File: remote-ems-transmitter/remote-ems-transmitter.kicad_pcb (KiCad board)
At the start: 2 copper layers, 65 x 30 mm, 59 parts, among them IC1 Wio-E5, J1 Conn_01x04_Pin, J2 Conn_01x02, J3 Conn_01x02, J4 Conn_Coaxial, J5 USB_C_Receptacle_USB2.0, J6 Conn_01x02_Pin, Q1 BSS138, SW1 SW_Push, SW2 SW_Push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

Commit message: LED周り修正
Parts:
- removed R21: 1k, Resistor_SMD:R_0603_1608Metric_Pad0.98x0.95mm_HandSolder
- added BAR2: OSX40601-AO, 0Ikedalibrary:OSX40601-AO, B.Cu at (36.1, 23.1)
- added D2: LED, LED_THT:LED_D5.0mm_FlatTop, B.Cu at (26.9, 35.7)
- BAR1: value HDSP-4830_2 -> OSX05201-GGR1; footprint Display:HDSP-4830 -> 0Ikedalibrary:OSX05201-GGR1
- D1: footprint LED_SMD:LED_0603_1608Metric_Pad1.05x0.95mm_HandSolder -> LED_THT:LED_D5.0mm_FlatTop
- R3: value 4.7k -> 100; moved to B.Cu
- SW4: moved to B.Cu
- moved R3 34.0 mm to (63.0, 36.4), turned to 0 degrees
- moved D1 22.6 mm to (37.7, 35.7), turned to 90 degrees
- moved J6 14.2 mm to (27.1, 29.5)
- moved BAR1 11.7 mm to (44.2, 22.4)
- moved C11 9.43 mm to (29.0, 43.4), turned to 180 degrees
- moved R4 7.85 mm to (42.4, 24.0), turned to 0 degrees
- moved R11 6.41 mm to (42.4, 25.6), turned to 0 degrees
- moved C14 5.20 mm to (20.6, 29.6)
- moved C15 5.20 mm to (20.6, 36.0)
- moved U5 5.00 mm to (20.8, 32.8)
- moved U3 4.93 mm to (29.0, 40.2), turned to -90 degrees
- moved C12 4.84 mm to (17.2, 29.6)
- moved C13 4.84 mm to (17.2, 36.0)
- moved U4 4.84 mm to (17.1, 32.8)
- moved R19 4.57 mm to (37.2, 30.8), turned to 0 degrees
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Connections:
- BAR1 pad 10: LED_opt_supply9 -> Net-(BAR1-K-Pad10)
- BAR1 pad 6: LED_opt_supply5 -> Net-(BAR1-K-Pad6)
- BAR1 pad 7: LED_opt_supply6 -> Net-(BAR1-K-Pad7)
- BAR1 pad 8: LED_opt_supply7 -> Net-(BAR1-K-Pad8)
- BAR1 pad 9: LED_opt_supply8 -> Net-(BAR1-K-Pad9)
- D1 pad 2: Net-(D1-A) -> VBUS
- Q1 pad 1: Wio-RST -> Net-(Q1-G)
- R11 pad 1: Net-(BAR1-K-Pad13) -> Net-(BAR2-K-Pad6)
- R11 pad 2: GNDD -> SW
- R12 pad 1: Net-(BAR1-K-Pad14) -> Net-(BAR2-A-Pad4)
- R12 pad 2: GNDD -> SW
- R13 pad 1: Net-(BAR1-K-Pad15) -> Net-(BAR2-A-Pad2)
- R13 pad 2: GNDD -> SW
- R14 pad 1: Net-(BAR1-K-Pad16) -> Net-(BAR1-K-Pad6)
- R15 pad 1: Net-(BAR1-K-Pad17) -> Net-(BAR1-K-Pad7)
- R16 pad 1: Net-(BAR1-K-Pad18) -> Net-(BAR1-K-Pad8)
- R17 pad 1: Net-(BAR1-K-Pad19) -> Net-(BAR1-K-Pad9)
- R18 pad 1: Net-(BAR1-K-Pad20) -> Net-(BAR1-K-Pad10)
- R3 pad 1: Net-(BAR1-K-Pad11) -> Wio-RST
- R3 pad 2: GNDD -> Net-(Q1-G)
- R4 pad 1: Net-(BAR1-K-Pad12) -> Net-(BAR2-K-Pad8)
- R4 pad 2: GNDD -> SW
- R8 pad 1: Wio-RST -> Net-(Q1-G)
- U1 pad 20: LED_opt_supply5 -> unconnected-(U1-PA10-Pad20)
- U1 pad 21: LED_opt_supply6 -> unconnected-(U1-PA11-Pad21)
- U1 pad 22: LED_opt_supply7 -> unconnected-(U1-PA12-Pad22)
- U1 pad 25: LED_opt_supply9 -> unconnected-(U1-PA15-Pad25)
- U1 pad 26: LED_opt_supply8 -> unconnected-(U1-PB3-Pad26)
- U1 pad 28: LED2 -> unconnected-(U1-PB5-Pad28)
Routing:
- net +3.3V: track 86.6 -> 137.3 mm
- net SW: track 20.8 -> 42.8 mm, vias 0 -> 2
- net LED1: track 0.00 -> 18.0 mm, vias 0 -> 2
- net UART_RX: track 8.77 -> 24.8 mm, vias 0 -> 1
- net LED_opt_supply8: track 15.7 -> 0.00 mm, vias 1 -> 0
- net LED_opt_supply9: track 15.5 -> 0.00 mm, vias 1 -> 0
- net UART_TX: track 6.91 -> 22.0 mm, vias 0 -> 1
- net LED_opt_supply7: track 12.7 -> 0.00 mm
- net LED_opt_supply6: track 11.0 -> 0.00 mm
- net Net-(BAR2-K-Pad8): track 0.00 -> 10.4 mm
- net STAT: track 18.3 -> 7.96 mm, vias 1 -> 2
- net LED_opt_supply5: track 9.24 -> 0.00 mm
- net +BATT: track 44.0 -> 52.0 mm
- net Net-(BAR2-A-Pad2): track 0.00 -> 7.93 mm
- net Wio-RST: track 22.3 -> 16.8 mm
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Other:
- board text added: "R T"
- board text added: "RST"
- board text added: "UART"

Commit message: LED仕様変更
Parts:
- added Q2: BSS138, Package_TO_SOT_SMD:SOT-23, F.Cu at (41.6, 30.6)
- added R21: 100, Resistor_SMD:R_0603_1608Metric_Pad0.98x0.95mm_HandSolder, F.Cu at (45.3, 30.5)
- added R22: 10k, Resistor_SMD:R_0603_1608Metric_Pad0.98x0.95mm_HandSolder, F.Cu at (45.3, 28.9)
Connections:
- BAR2 pad 3: +3.3V -> Net-(BAR2-A-Pad3)
- BAR2 pad 4: Net-(BAR2-A-Pad4) -> +3.3V
- BAR2 pad 7: +3.3V -> Net-(BAR2-K-Pad7)
- BAR2 pad 8: Net-(BAR2-K-Pad8) -> +3.3V
- R11 pad 2: SW -> Net-(Q2-S)
- R12 pad 1: Net-(BAR2-A-Pad4) -> Net-(BAR2-A-Pad3)
- R12 pad 2: SW -> Net-(Q2-S)
- R13 pad 2: SW -> Net-(Q2-S)
- R4 pad 1: Net-(BAR2-K-Pad8) -> Net-(BAR2-K-Pad7)
- R4 pad 2: SW -> Net-(Q2-S)
- U1 pad 20: unconnected-(U1-PA10-Pad20) -> emergency_stop_LED
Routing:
- net SW: track 42.8 -> 20.8 mm, vias 2 -> 0
- net Net-(BAR2-K-Pad8): track 10.4 -> 0.00 mm
- net Net-(Q2-S): track 0.00 -> 9.17 mm
- net Net-(BAR2-K-Pad7): track 0.00 -> 7.86 mm
- net Net-(BAR2-A-Pad3): track 0.00 -> 4.74 mm
- net Net-(Q2-G): track 0.00 -> 3.88 mm
- net emergency_stop_LED: track 0.00 -> 2.52 mm
- net Net-(BAR2-A-Pad4): track 2.20 -> 0.00 mm
- net +3.3V: track 137.3 -> 138.8 mm
- net GNDD: vias 37 -> 41

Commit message: ビア打ち、シルク修正中　残りは別日に対応します
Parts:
- added D3: LED, LED_SMD:LED_0603_1608Metric_Pad1.05x0.95mm_HandSolder, F.Cu at (29.4, 41.6)
- added G***: LOGO, LOGO, B.Cu at (66.2, 22.4)
- added R23: 1k, Resistor_SMD:R_0603_1608Metric_Pad0.98x0.95mm_HandSolder, F.Cu at (29.4, 38.2)
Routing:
- net VBUS: track 38.1 -> 42.9 mm
- net Net-(D3-A): track 0.00 -> 1.61 mm
- net GNDD: vias 41 -> 106
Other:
- board text added: "LED"
- board text added: "USB"
- board text added: "remote-ems-transmitter version 1.0 create by ikeda"
- board text added: "充電"

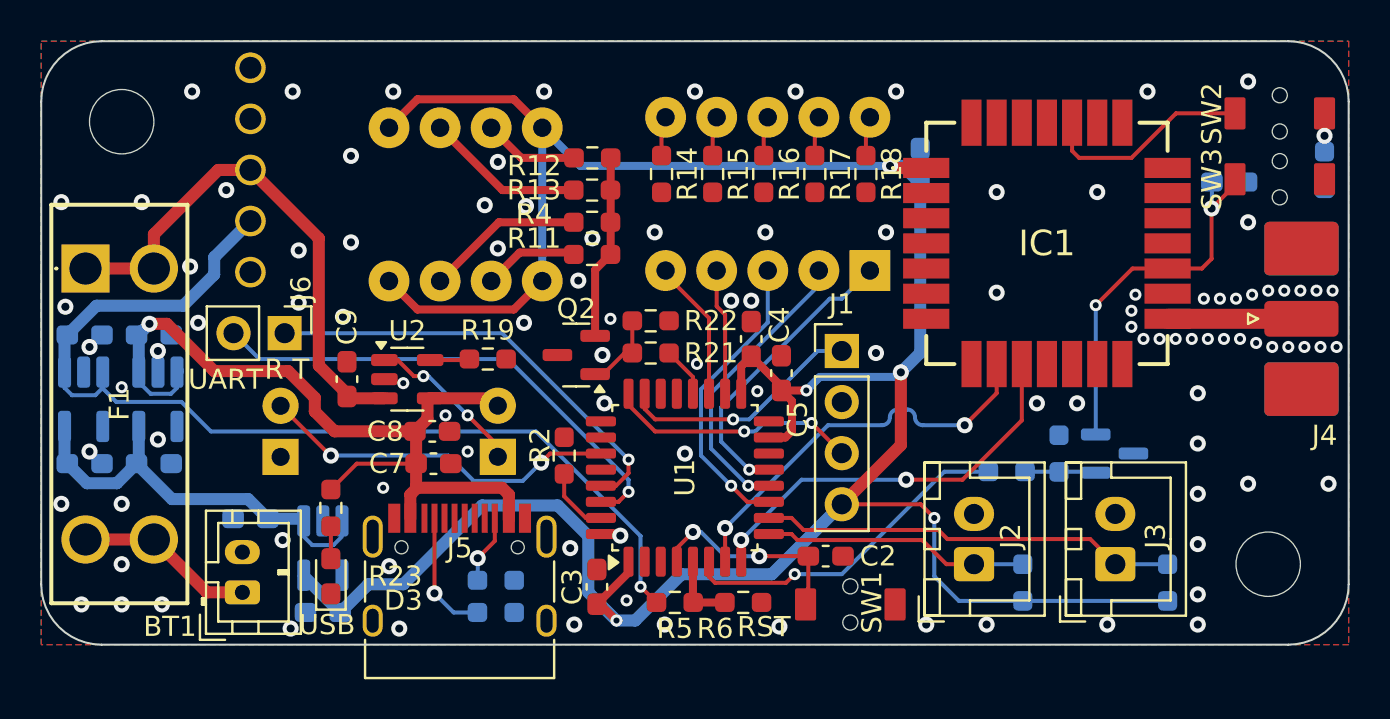
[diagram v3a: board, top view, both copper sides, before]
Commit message: FETの向きを修正 ガーバー出力
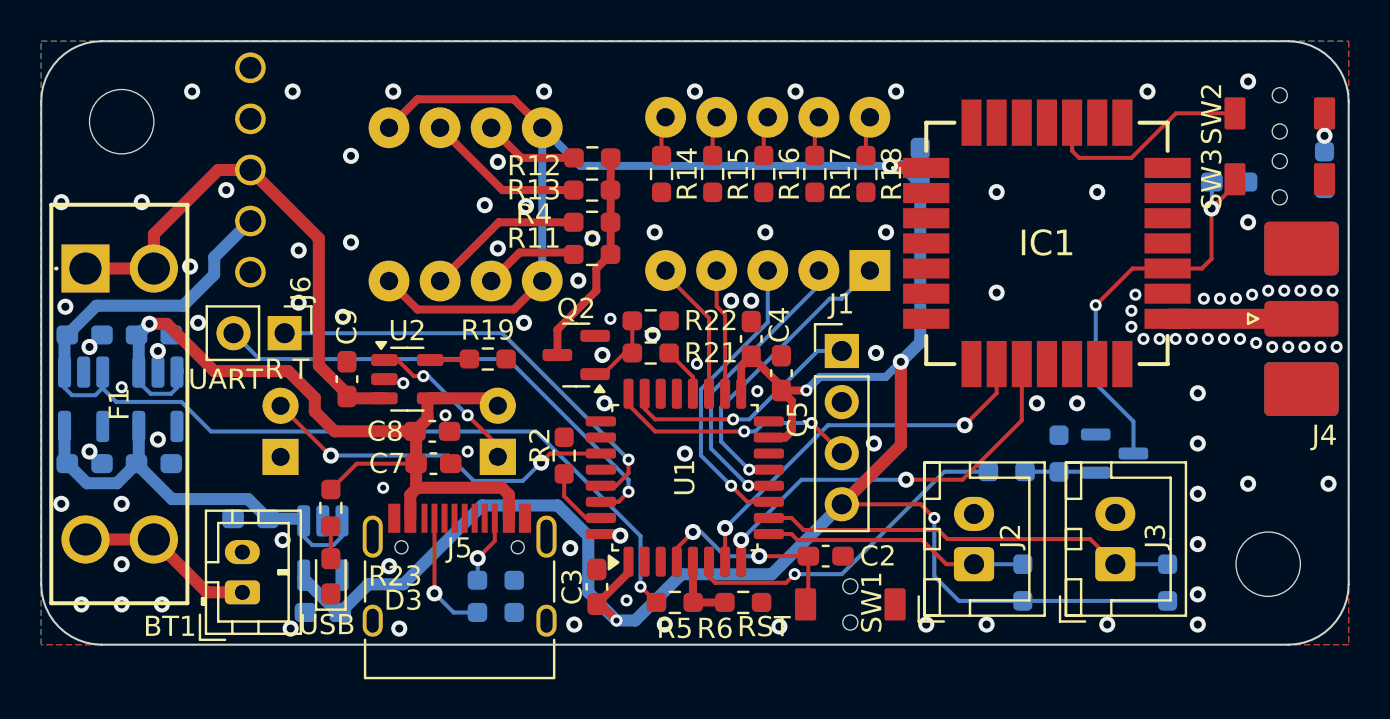
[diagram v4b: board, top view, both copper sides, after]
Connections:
- Q1 pad 2: Net-(IC1-RST) -> GNDD
- Q1 pad 3: GNDD -> Net-(IC1-RST)
- Q2 pad 2: Net-(Q2-S) -> GNDD
- Q2 pad 3: GNDD -> Net-(Q2-D)
- R11 pad 2: Net-(Q2-S) -> Net-(Q2-D)
- R12 pad 2: Net-(Q2-S) -> Net-(Q2-D)
- R13 pad 2: Net-(Q2-S) -> Net-(Q2-D)
- R4 pad 2: Net-(Q2-S) -> Net-(Q2-D)
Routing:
- net Net-(Q2-D): track 0.00 -> 10.9 mm
- net Net-(Q2-S): track 9.17 -> 0.00 mm
- net Net-(IC1-RST): track 18.9 -> 20.6 mm
- net Wio_TX: track 20.2 -> 19.4 mm
- net GNDD: vias 106 -> 108
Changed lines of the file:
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@@
 	(net 79 "unconnected-(U1-PA11-Pad21)")
 	(net 80 "unconnected-(U1-PA15-Pad25)")
-	(net 81 "Net-(Q2-S)")
+	(net 81 "Net-(Q2-D)")
 	(net 82 "Net-(Q2-G)")
 	(net 83 "emergency_stop_LED")
@@
 			(layers "F.Cu" "F.Paste" "F.Mask")
 			(roundrect_rratio 0.25)
-			(net 81 "Net-(Q2-S)")
+			(net 81 "Net-(Q2-D)")
 			(pintype "passive")
 		)
@@
 			(layers "F.Cu" "F.Paste" "F.Mask")
 			(roundrect_rratio 0.25)
-			(net 81 "Net-(Q2-S)")
+			(net 81 "Net-(Q2-D)")
 			(pintype "passive")
 		)
@@
 			(layers "F.Cu" "F.Paste" "F.Mask")
 			(roundrect_rratio 0.25)
-			(net 81 "Net-(Q2-S)")
+			(net 81 "Net-(Q2-D)")
 			(pintype "passive")
 		)
@@
 			(layers "F.Cu" "F.Paste" "F.Mask")
 			(roundrect_rratio 0.25)
-			(net 81 "Net-(Q2-S)")
+			(net 7 "GNDD")
 			(pinfunction "S")
 			(pintype "passive")
@@
 			(layers "F.Cu" "F.Paste" "F.Mask")
 			(roundrect_rratio 0.25)
-			(net 7 "GNDD")
+			(net 81 "Net-(Q2-D)")
 			(pinfunction "D")
 			(pintype "passive")
@@
 			(layers "F.Cu" "F.Paste" "F.Mask")
 			(roundrect_rratio 0.25)
-			(net 81 "Net-(Q2-S)")
+			(net 81 "Net-(Q2-D)")
 			(pintype "passive")
 		)
@@
 			(layers "B.Cu" "B.Paste" "B.Mask")
 			(roundrect_rratio 0.25)
-			(net 10 "Net-(IC1-RST)")
+			(net 7 "GNDD")
 			(pinfunction "S")
 			(pintype "passive")
@@
 			(layers "B.Cu" "B.Paste" "B.Mask")
 			(roundrect_rratio 0.25)
-			(net 7 "GNDD")
+			(net 10 "Net-(IC1-RST)")
 			(pinfunction "D")
 			(pintype "passive")
@@
 	)
 	(via
+		(at 56.4 35)
+		(size 0.8)
+		(drill 0.4)
+		(layers "F.Cu" "B.Cu")
+		(free yes)
+		(net 7)
+	)
+	(via
 		(at 72.5 37.5)
 		(size 0.8)
@@
 	)
 	(via
+		(at 45.4 29.6)
+		(size 0.8)
+		(drill 0.4)
+		(layers "F.Cu" "B.Cu")
+		(free yes)
+		(net 7)
+	)
+	(via
 		(at 20.8 30.4)
 		(size 0.8)
@@
 	)
 	(segment
+		(start 57.7375 30.9375)
+		(end 57.7375 35.0825)
+		(width 0.6)
+		(layer "F.Cu")
+		(net 8)
+	)
+	(segment
 		(start 32.29 26.922)
 		(end 33.706 28.338)
@@
 	)
 	(segment
-		(start 57.7375 31.4625)
-		(end 57.7375 35.0825)
-		(width 0.6)
-		(layer "F.Cu")
-		(net 8)
-	)
-	(segment
 		(start 44.2 40.875)
 		(end 44.2 41.4125)
@@
 	)
 	(via
-		(at 57.7375 31.4625)
+		(at 57.7375 30.9375)
 		(size 0.8)
 		(drill 0.4)
@@
 	)
 	(segment
-		(start 58.7 30.5)
-		(end 58.7 22.0625)
+		(start 29.73125 43.4)
+		(end 29.8625 43.4)
 		(width 0.6)
 		(layer "B.Cu")
@@
 	)
 	(segment
-		(start 53.0375 32.3625)
-		(end 53.71 31.69)
-		(width 0.4)
+		(start 36.92 38.08)
+		(end 33 42)
+		(width 0.6)
 		(layer "B.Cu")
 		(net 8)
@@
 	(segment
 		(start 28.05 41.55)
-		(end 28.05 41.5875)
+		(end 28.05 41.71875)
 		(width 0.6)
 		(layer "B.Cu")
@@
 	)
 	(segment
-		(start 53.71 31.69)
-		(end 57.51 31.69)
-		(width 0.4)
+		(start 42.2 42.4)
+		(end 42.2 39.6)
+		(width 0.6)
 		(layer "B.Cu")
 		(net 8)
 	)
 	(segment
-		(start 36.92 38.08)
-		(end 33 42)
+		(start 57.7375 30.9375)
+		(end 58.7 29.975)
 		(width 0.6)
 		(layer "B.Cu")
@@
 	)
 	(segment
-		(start 57.51 31.69)
-		(end 57.7375 31.4625)
+		(start 56.985 31.69)
+		(end 53.71 31.69)
 		(width 0.4)
 		(layer "B.Cu")
@@
 	)
 	(segment
-		(start 42.2 42.4)
-		(end 42.2 39.6)
-		(width 0.6)
-		(layer "B.Cu")
-		(net 8)
-	)
-	(segment
 		(start 59.4 41.6)
 		(end 60.625 42.825)
@@
 	)
 	(segment
+		(start 57.7375 30.9375)
+		(end 56.985 31.69)
+		(width 0.4)
+		(layer "B.Cu")
+		(net 8)
+	)
+	(segment
 		(start 59.4 38.7)
 		(end 59.4 41.6)
@@
 	)
 	(segment
+		(start 53.71 31.69)
+		(end 53.0375 32.3625)
+		(width 0.4)
+		(layer "B.Cu")
+		(net 8)
+	)
+	(segment
 		(start 60.625 42.825)
 		(end 63.8 42.825)
@@
 	)
 	(segment
-		(start 57.7375 31.4625)
-		(end 58.7 30.5)
-		(width 0.6)
-		(layer "B.Cu")
-		(net 8)
-	)
-	(segment
 		(start 39.91 19.302)
 		(end 41.808 21.2)
@@
 	)
 	(segment
-		(start 28.05 41.5875)
-		(end 29.8625 43.4)
+		(start 28.05 41.71875)
+		(end 29.73125 43.4)
 		(width 0.6)
 		(layer "B.Cu")
@@
 	)
 	(segment
+		(start 58.7 29.975)
+		(end 58.7 22.0625)
+		(width 0.6)
+		(layer "B.Cu")
+		(net 8)
+	)
+	(segment
 		(start 53.1375 42.2125)
 		(end 52.75 42.6)
@@
 	)
 	(segment
+		(start 67.425 32.025)
+		(end 69.3 33.9)
+		(width 0.2)
+		(layer "B.Cu")
+		(net 10)
+	)
+	(segment
 		(start 73.2 22)
 		(end 73.2 23.3)
@@
 	)
 	(segment
+		(start 67.425 28.125)
+		(end 67.425 32.025)
+		(width 0.2)
+		(layer "B.Cu")
+		(net 10)
+	)
+	(segment
 		(start 73.2 23.3)
 		(end 73.186 23.314)
@@
 	)
 	(segment
-		(start 67.425 28.125)
-		(end 67.425 34.55)
+		(start 69.3 33.9)
+		(end 69.3 35.5)
 		(width 0.2)
 		(layer "B.Cu")
@@
 	)
 	(segment
-		(start 58.83 34.09)
-		(end 60.91 34.09)
-		(width 0.2)
-		(layer "B.Cu")
-		(net 29)
-	)
-	(segment
-		(start 57.58 33.31)
-		(end 58.05 33.31)
-		(width 0.2)
-		(layer "B.Cu")
-		(net 29)
-	)
-	(segment
 		(start 49 39.2)
 		(end 54.11 34.09)
@@
 	(segment
 		(start 54.11 34.09)
-		(end 56.8 34.09)
-		(width 0.2)
-		(layer "B.Cu")
-		(net 29)
-	)
-	(arc
-		(start 58.44 33.7)
-		(mid 58.554228 33.975772)
-		(end 58.83 34.09)
-		(width 0.2)
-		(layer "B.Cu")
-		(net 29)
-	)
-	(arc
-		(start 56.8 34.09)
-		(mid 57.075772 33.975772)
-		(end 57.19 33.7)
-		(width 0.2)
-		(layer "B.Cu")
-		(net 29)
-	)
-	(arc
-		(start 58.05 33.31)
-		(mid 58.325772 33.424228)
-		(end 58.44 33.7)
-		(width 0.2)
-		(layer "B.Cu")
-		(net 29)
-	)
-	(arc
-		(start 57.19 33.7)
-		(mid 57.304228 33.424228)
-		(end 57.58 33.31)
+		(end 60.91 34.09)
 		(width 0.2)
 		(layer "B.Cu")
@@
 	)
 	(segment
-		(start 43.3125 25.5875)
-		(end 43.3 25.6)
+		(start 40.6625 29.3375)
+		(end 40.6625 30.6)
 		(width 0.4)
 		(layer "F.Cu")
@@
 	)
 	(segment
-		(start 42.5375 26.3625)
-		(end 42.5375 29.65)
+		(start 42.6 27.4)
+		(end 40.6625 29.3375)
 		(width 0.4)
 		(layer "F.Cu")
@@
 	)
 	(segment
-		(start 43.3 25.6)
-		(end 42.5375 26.3625)
+		(start 43.3125 25.5875)
+		(end 42.6 26.3)
 		(width 0.4)
 		(layer "F.Cu")
@@
 	)
 	(segment
+		(start 42.6 26.3)
+		(end 42.6 27.4)
+		(width 0.4)
+		(layer "F.Cu")
+		(net 81)
+	)
+	(segment
 		(start 44.3875 28.9)
 		(end 44.3875 30.5)
@@
 		)
 	)
-	(generated
-		(type tuning_pattern)
-		(name "Tuning Pattern")
-		(layer "B.Cu")
-		(base_line
-			(pts
-				(xy 56.8 34.09) (xy 60.2 34.09)
-			)
-		)
-		(corner_radius_percent 80)
-		(end
-			(xy 60.2 34.09)
-		)
-		(initial_side "left")
-		(last_diff_pair_gap 0.18)
-		(last_netname "Wio_TX")
-		(last_status "tuned")
-		(last_track_width 0.2)
-		(last_tuning "23.3807 mm (調整済み)")
-		(max_amplitude 0.78)
-		(min_amplitude 0.2)
-		(min_spacing 1.25)
-		(origin
-			(xy 56.8 34.09)
-		)
-		(override_custom_rules no)
-		(rounded yes)
-		(single_sided no)
-		(target_length 1000000)
-		(target_length_max 1000000)
-		(target_length_min 0)
-		(target_skew 0)
-		(target_skew_max 0.1)
-		(target_skew_min -0.1)
-		(tuning_mode "single")
-		(members 191be3ec-bd7a-4197-b52d-abbc0183a6cd 1ceb83d9-309a-466f-8203-879a6ecf75d6
-			4ea0a97e-16e6-4886-ae13-930ba0ef418e c9a52f39-7c29-4efa-be46-2d67c93914e1
-			dffd05e8-288e-4171-8229-b4f78fd29e9b
-		)
-	)
